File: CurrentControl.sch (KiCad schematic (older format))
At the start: 7 parts

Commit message: Annotated sheets
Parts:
- gave numbers to parts that had none: 7
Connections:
- net at Q301.3 (S), R303.1: now also U201.6 (-); no longer U201.2 (-)
- net at R302.2: now also U201.7; no longer U201.1
- net at R301.1, RV301.3: now also U201.5 (+); no longer U201.3 (+)
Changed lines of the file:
@@
 $EndDescr
 $Comp
-L R R?
+L R R303
 U 1 1 56A5BC2B
 P 8350 5300
-F 0 "R?" V 8430 5300 50  0000 C CNN
+F 0 "R303" V 8430 5300 50  0000 C CNN
 F 1 ".1" V 8350 5300 50  0000 C CNN
 F 2 "" V 8280 5300 30  0000 C CNN
@@
 $EndComp
 $Comp
-L LMV358 U?
-U 1 1 56A5BC38
+L LMV358 U201
+U 2 1 56A5BC38
 P 5800 4200
-F 0 "U?" H 5750 4400 60  0000 L CNN
+F 0 "U201" H 5750 4400 60  0000 L CNN
 F 1 "LMV358" H 5750 3950 60  0000 L CNN
 F 2 "" H 5800 4200 60  0000 C CNN
 F 3 "" H 5800 4200 60  0000 C CNN
-	1    5800 4200
+	2    5800 4200
 	1    0    0    -1
 $EndComp
 $Comp
-L Q_NMOS_DGS Q?
+L Q_NMOS_DGS Q301
 U 1 1 56A5BC40
 P 8250 4200
-F 0 "Q?" H 8550 4250 50  0000 R CNN
+F 0 "Q301" H 8550 4250 50  0000 R CNN
 F 1 "BUK9575" H 8900 4150 50  0000 R CNN
 F 2 "" H 8450 4300 50  0000 C CNN
@@
 $EndComp
 $Comp
-L R R?
+L R R301
 U 1 1 56A5BC47
 P 3800 5150
-F 0 "R?" V 3880 5150 50  0000 C CNN
+F 0 "R301" V 3880 5150 50  0000 C CNN
 F 1 "R" V 3800 5150 50  0000 C CNN
 F 2 "" V 3730 5150 50  0000 C CNN
@@
 $EndComp
 $Comp
-L GND #PWR?
+L GND #PWR302
 U 1 1 56A5BC4E
 P 5700 4700
-F 0 "#PWR?" H 5700 4450 50  0001 C CNN
+F 0 "#PWR302" H 5700 4450 50  0001 C CNN
 F 1 "GND" H 5700 4550 50  0000 C CNN
 F 2 "" H 5700 4700 60  0000 C CNN
@@
 $EndComp
 $Comp
-L POT RV?
+L POT RV301
 U 1 1 56A5BC54
 P 3800 4350
-F 0 "RV?" H 3800 4250 50  0000 C CNN
+F 0 "RV301" H 3800 4250 50  0000 C CNN
 F 1 "POT" H 3800 4350 50  0000 C CNN
 F 2 "" H 3800 4350 50  0000 C CNN
@@
 $EndComp
 $Comp
-L C C?
+L C C301
 U 1 1 56A5BC5B
 P 5000 3500
-F 0 "C?" H 5025 3600 50  0000 L CNN
+F 0 "C301" H 5025 3600 50  0000 L CNN
 F 1 "C" H 5025 3400 50  0000 L CNN
 F 2 "" H 5038 3350 50  0000 C CNN
@@
 $EndComp
 $Comp
-L GND #PWR?
+L GND #PWR301
 U 1 1 56A5BC62
 P 5000 3800
-F 0 "#PWR?" H 5000 3550 50  0001 C CNN
+F 0 "#PWR301" H 5000 3550 50  0001 C CNN
 F 1 "GND" H 5000 3650 50  0000 C CNN
 F 2 "" H 5000 3800 50  0000 C CNN
@@
 	8350 2100 9150 2100
 $Comp
-L R R?
+L R R302
 U 1 1 56A5BE98
 P 6700 4200
-F 0 "R?" V 6780 4200 50  0000 C CNN
+F 0 "R302" V 6780 4200 50  0000 C CNN
 F 1 "1k" V 6700 4200 50  0000 C CNN
 F 2 "" V 6630 4200 50  0000 C CNN

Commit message: Updated BOM
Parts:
- added P301: HEATSINK, current:FA-T220-38E, symbol CONN_01X01
- C301: footprint (none) -> Capacitors_SMD:C_0805_HandSoldering
- Q301: footprint (none) -> TO_SOT_Packages_THT:TO-220_Neutral123_Vertical
- R301: value R -> 68k; footprint (none) -> Resistors_SMD:R_0805_HandSoldering
- R302: footprint (none) -> Resistors_SMD:R_0805_HandSoldering
- R303: footprint (none) -> Resistors_ThroughHole:Resistor_Horizontal_RM15mm
- RV301: value POT -> 10K; footprint (none) -> current:P090L-02F25BR10K; symbol POT -> POT-RESCUE-CurrentSinkOrSwim
- U201: footprint (none) -> SMD_Packages:SOIC-8-N; MPN (none) -> LMV3581DT
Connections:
- net 2.7V: now also R301.1; no longer RV301.2
- net Current_Sink-: now also RV301.3; no longer R301.2
- net at RV301.1: now also R301.2, U201.5 (+)
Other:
- moved on the sheet: R301, RV301
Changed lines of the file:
@@
 EESchema Schematic File Version 2
+LIBS:CurrentSinkOrSwim-rescue
 LIBS:power
 LIBS:device
@@
 F 0 "R303" V 8430 5300 50  0000 C CNN
 F 1 ".1" V 8350 5300 50  0000 C CNN
-F 2 "" V 8280 5300 30  0000 C CNN
+F 2 "Resistors_ThroughHole:Resistor_Horizontal_RM15mm" V 8280 5300 30  0001 C CNN
 F 3 "" H 8350 5300 30  0000 C CNN
 F 4 "AC01000001007JA100" V 8350 5300 60  0001 C CNN "MPN"
@@
 F 0 "U201" H 5750 4400 60  0000 L CNN
 F 1 "LMV358" H 5750 3950 60  0000 L CNN
-F 2 "" H 5800 4200 60  0000 C CNN
+F 2 "SMD_Packages:SOIC-8-N" H 5800 4200 60  0001 C CNN
 F 3 "" H 5800 4200 60  0000 C CNN
+F 4 "LMV3581DT" H 5800 4200 60  0001 C CNN "MPN"
 	2    5800 4200
 	1    0    0    -1
@@
 F 0 "Q301" H 8550 4250 50  0000 R CNN
 F 1 "BUK9575" H 8900 4150 50  0000 R CNN
-F 2 "" H 8450 4300 50  0000 C CNN
+F 2 "TO_SOT_Packages_THT:TO-220_Neutral123_Vertical" H 8450 4300 50  0001 C CNN
 F 3 "" H 8250 4200 50  0000 C CNN
 F 4 "BUK9575-100A,127" H 8250 4200 60  0001 C CNN "MPN"
@@
 L R R301
 U 1 1 56A5BC47
-P 3800 5150
-F 0 "R301" V 3880 5150 50  0000 C CNN
-F 1 "R" V 3800 5150 50  0000 C CNN
-F 2 "" V 3730 5150 50  0000 C CNN
-F 3 "" H 3800 5150 50  0000 C CNN
-	1    3800 5150
-	1    0    0    -1
-$EndComp
-$Comp
-L GND #PWR302
+P 3950 4500
+F 0 "R301" V 4030 4500 50  0000 C CNN
+F 1 "68k" V 3950 4500 50  0000 C CNN
+F 2 "Resistors_SMD:R_0805_HandSoldering" V 3880 4500 50  0001 C CNN
+F 3 "" H 3950 4500 50  0000 C CNN
+	1    3950 4500
+	1    0    0    -1
+$EndComp
+$Comp
+L GND #PWR05
 U 1 1 56A5BC4E
 P 5700 4700
-F 0 "#PWR302" H 5700 4450 50  0001 C CNN
+F 0 "#PWR05" H 5700 4450 50  0001 C CNN
 F 1 "GND" H 5700 4550 50  0000 C CNN
 F 2 "" H 5700 4700 60  0000 C CNN
@@
 $EndComp
 $Comp
-L POT RV301
+L POT-RESCUE-CurrentSinkOrSwim RV301
 U 1 1 56A5BC54
-P 3800 4350
-F 0 "RV301" H 3800 4250 50  0000 C CNN
-F 1 "POT" H 3800 4350 50  0000 C CNN
-F 2 "" H 3800 4350 50  0000 C CNN
-F 3 "" H 3800 4350 50  0000 C CNN
-	1    3800 4350
+P 3800 5050
+AR Path="/56A5BC54" Ref="RV301"  Part="1"
+AR Path="/56A5B91B/56A5BC54" Ref="RV301"  Part="1"
+F 0 "RV301" H 3800 4950 50  0000 C CNN
+F 1 "10K" H 3800 5050 50  0000 C CNN
+F 2 "current:P090L-02F25BR10K" H 3800 5050 50  0001 C CNN
+F 3 "" H 3800 5050 50  0000 C CNN
+	1    3800 5050
 	0    1    1    0
 $EndComp
@@
 F 0 "C301" H 5025 3600 50  0000 L CNN
 F 1 "C" H 5025 3400 50  0000 L CNN
-F 2 "" H 5038 3350 50  0000 C CNN
+F 2 "Capacitors_SMD:C_0805_HandSoldering" H 5038 3350 50  0001 C CNN
 F 3 "" H 5000 3500 50  0000 C CNN
 	1    5000 3500
@@
 $EndComp
 $Comp
-L GND #PWR301
+L GND #PWR06
 U 1 1 56A5BC62
 P 5000 3800
-F 0 "#PWR301" H 5000 3550 50  0001 C CNN
+F 0 "#PWR06" H 5000 3550 50  0001 C CNN
 F 1 "GND" H 5000 3650 50  0000 C CNN
 F 2 "" H 5000 3800 50  0000 C CNN
@@
 	5700 4700 5700 4600
 Wire Wire Line
-	3800 4600 3800 5000
-Wire Wire Line
 	6650 4950 5100 4950
 Wire Wire Line
@@
 Wire Wire Line
 	4650 4100 4650 4750
-Wire Wire Line
-	4650 4750 3800 4750
-Connection ~ 3800 4750
 Wire Wire Line
 	3950 3200 5700 3200
@@
 F 0 "R302" V 6780 4200 50  0000 C CNN
 F 1 "1k" V 6700 4200 50  0000 C CNN
-F 2 "" V 6630 4200 50  0000 C CNN
+F 2 "Resistors_SMD:R_0805_HandSoldering" V 6630 4200 50  0001 C CNN
 F 3 "" H 6700 4200 50  0000 C CNN
 	1    6700 4200
@@
 Wire Wire Line
 	8350 5900 8550 5900
+$Comp
+L CONN_01X01 P301
+U 1 1 56AE7614
+P 9700 4150
+F 0 "P301" H 9700 4250 50  0000 C CNN
+F 1 "HEATSINK" V 9800 4150 50  0000 C CNN
+F 2 "current:FA-T220-38E" H 9700 4150 50  0001 C CNN
+F 3 "" H 9700 4150 50  0000 C CNN
+F 4 "FA-T220-38E-ND" H 9700 4150 60  0001 C CNN "MPN"
+	1    9700 4150
+	1    0    0    -1
+$EndComp
+Wire Wire Line
+	4650 4750 3800 4750
+Wire Wire Line
+	3950 4750 3950 4650
+Wire Wire Line
+	3800 4750 3800 4800
+Connection ~ 3950 4750
 $EndSCHEMATC

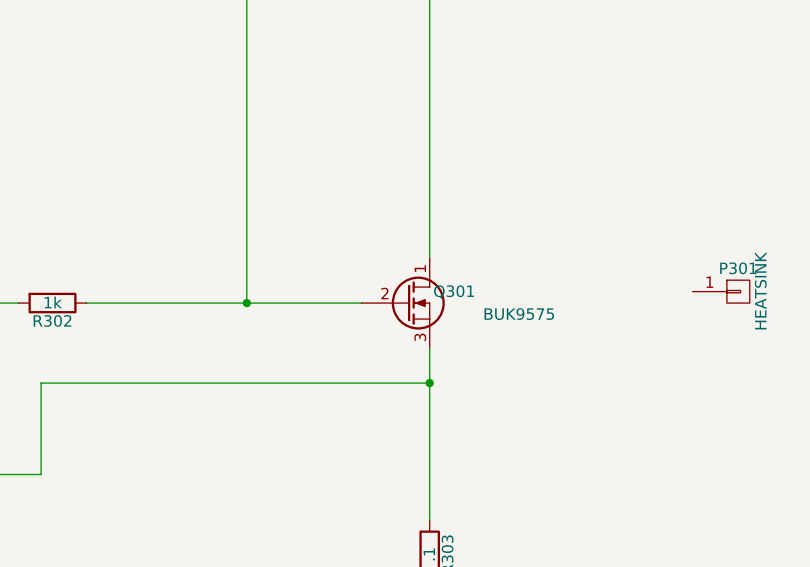
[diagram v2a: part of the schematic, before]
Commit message: This is the version of the file that has been submitted to OSH park
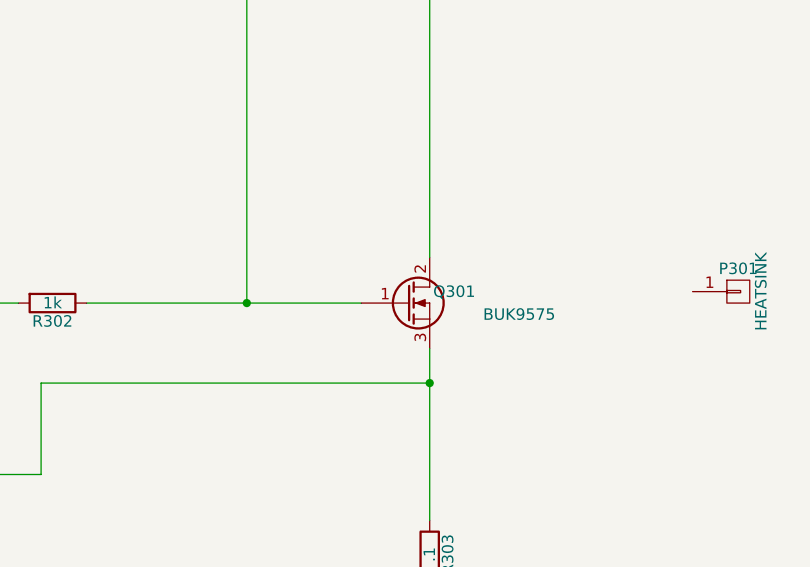
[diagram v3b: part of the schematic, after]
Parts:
- removed Q301: BUK9575, TO_SOT_Packages_THT:TO-220_Neutral123_Vertical, symbol Q_NMOS_DGS
- added Q301: BUK9575, current:TO-220_GDS_Vertical, symbol Q_NMOS_GDS
- RV301: MPN (none) -> P090L-02F25BR10K
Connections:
- net Current_Sink+: now also Q301.2 (D)
- net FET_Gate: now also Q301.1 (G)
- net at R303.1, U201.6 (-): now also Q301.3 (S)
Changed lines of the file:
@@
-$EndComp
-$Comp
-L Q_NMOS_DGS Q301
-U 1 1 56A5BC40
-P 8250 4200
-F 0 "Q301" H 8550 4250 50  0000 R CNN
-F 1 "BUK9575" H 8900 4150 50  0000 R CNN
-F 2 "TO_SOT_Packages_THT:TO-220_Neutral123_Vertical" H 8450 4300 50  0001 C CNN
-F 3 "" H 8250 4200 50  0000 C CNN
-F 4 "BUK9575-100A,127" H 8250 4200 60  0001 C CNN "MPN"
-	1    8250 4200
-	1    0    0    -1
 $EndComp
 $Comp
@@
 F 2 "current:P090L-02F25BR10K" H 3800 5050 50  0001 C CNN
 F 3 "" H 3800 5050 50  0000 C CNN
+F 4 "P090L-02F25BR10K" H 3800 5050 60  0001 C CNN "MPN"
 	1    3800 5050
 	0    1    1    0
@@
 	3800 4750 3800 4800
 Connection ~ 3950 4750
+$Comp
+L Q_NMOS_GDS Q301
+U 1 1 56D5A107
+P 8250 4200
+F 0 "Q301" H 8550 4250 50  0000 R CNN
+F 1 "BUK9575" H 8900 4150 50  0000 R CNN
+F 2 "current:TO-220_GDS_Vertical" H 8450 4300 50  0001 C CNN
+F 3 "" H 8250 4200 50  0000 C CNN
+F 4 "BUK9575-100A,127" H 8250 4200 60  0001 C CNN "MPN"
+	1    8250 4200
+	1    0    0    -1
+$EndComp
 $EndSCHEMATC
